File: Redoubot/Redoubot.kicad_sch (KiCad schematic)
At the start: 4 parts, among them U1 STM32G431RBTx, Y1 8MHz

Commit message: Added the footprints for the resistors, inductors and the crystal
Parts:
- Y1: footprint (none) -> Crystal:Crystal_SMD_HC49-SD
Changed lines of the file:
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@@
 			)
 		)
-		(property "Footprint" ""
+		(property "Footprint" "Crystal:Crystal_SMD_HC49-SD"
 			(at 34.29 49.53 0)
 			(hide yes)

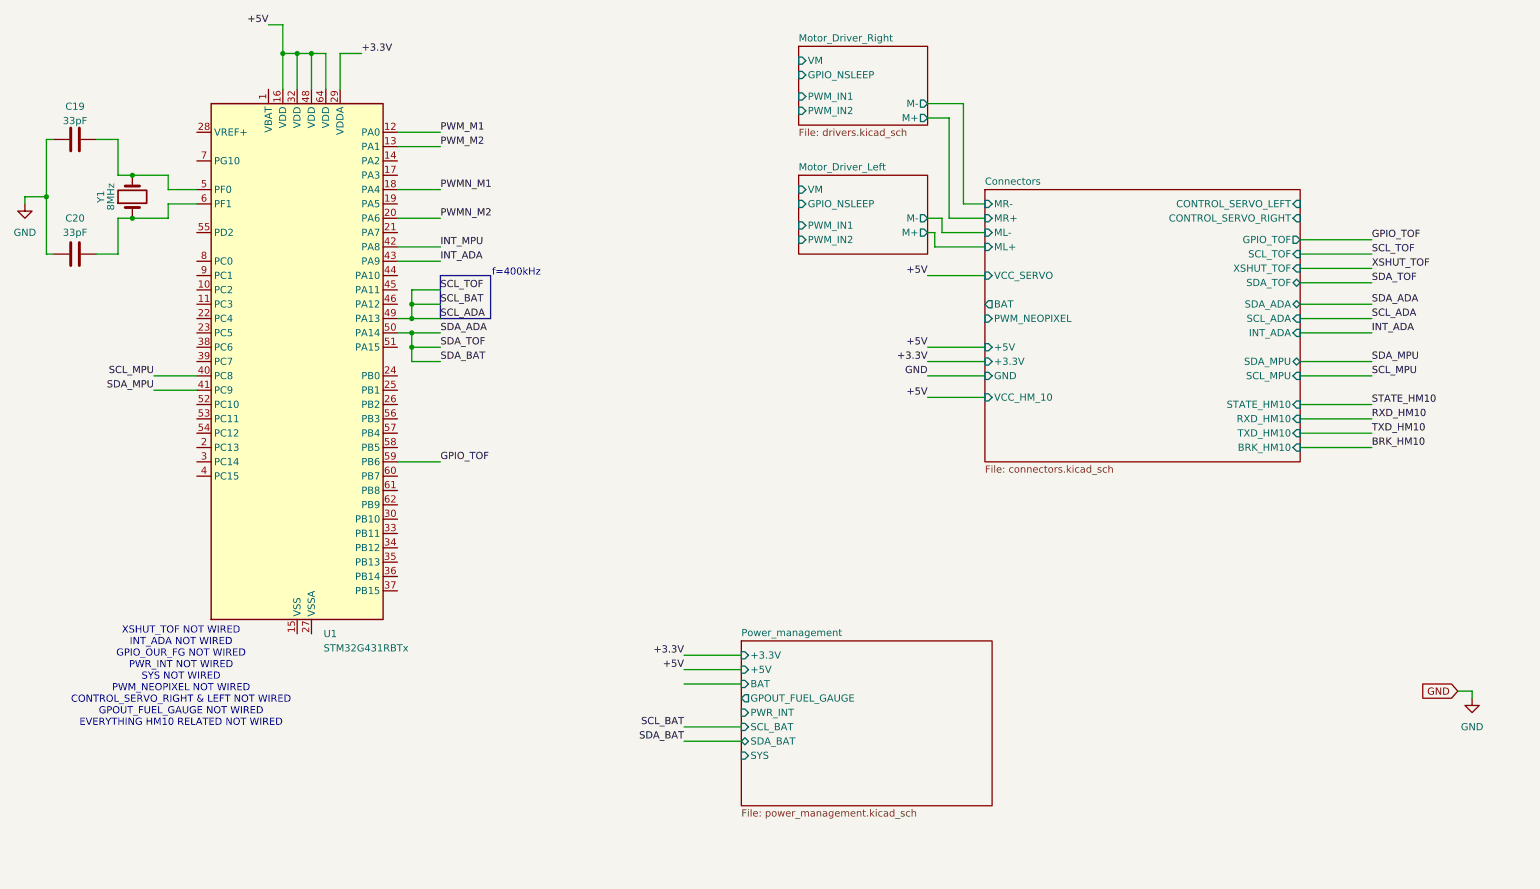
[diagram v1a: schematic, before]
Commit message: feat: added usb_c charging + flashing, added +3.3V generation, added HM10 & DFMini Support, wired everything and modified ioc accordingly
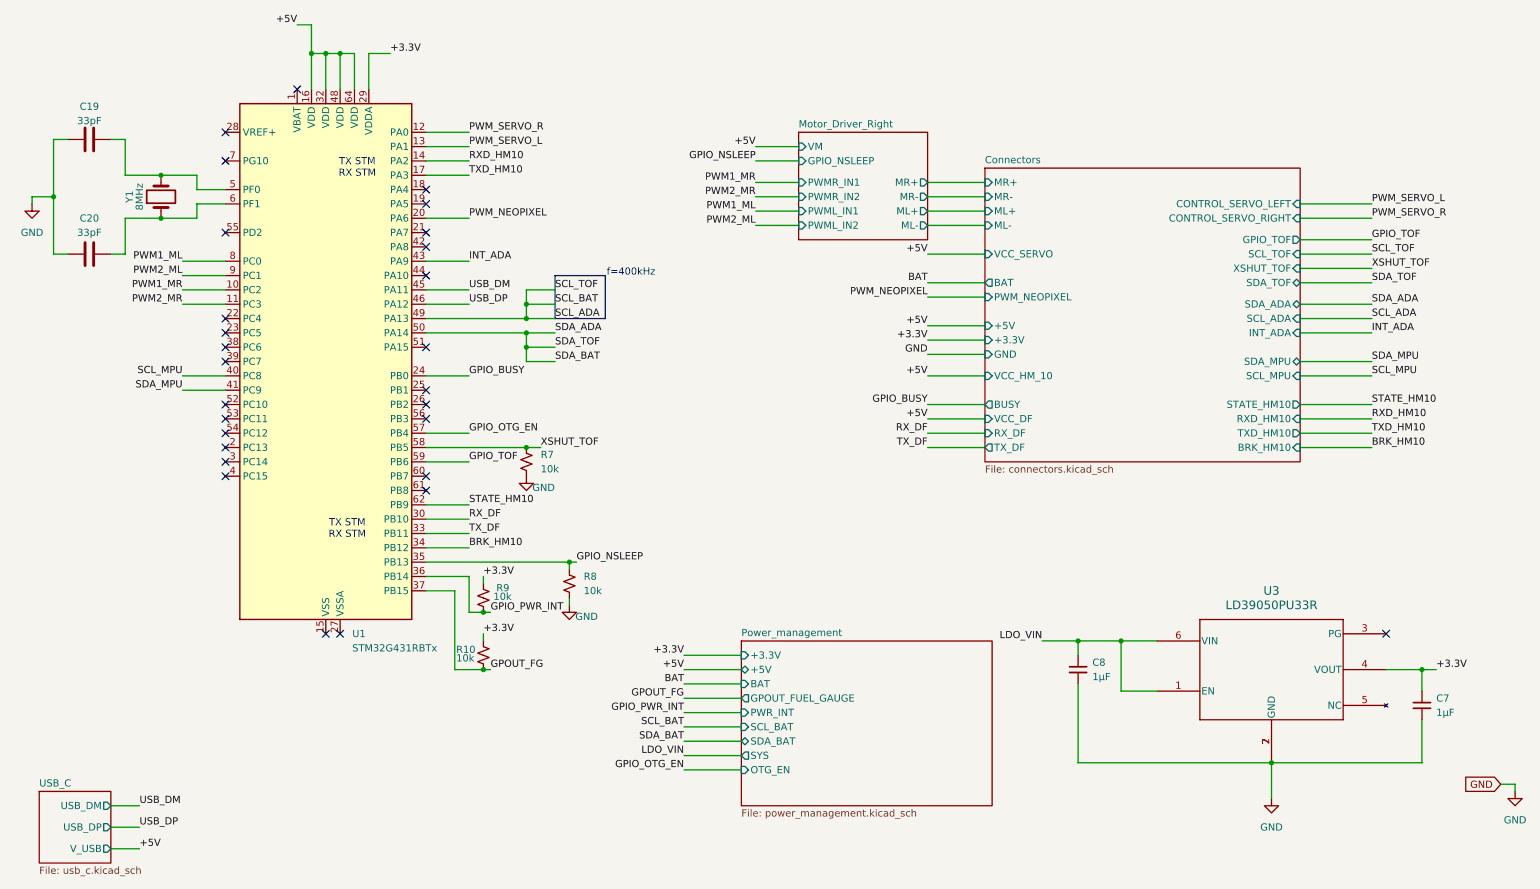
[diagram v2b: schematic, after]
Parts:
- added C7: 1µF, DFN6_3X3_STM, symbol Device:C_Small
- added C8: 1µF, symbol Device:C_Small
- added R10, R7, R8, R9: 10k, symbol Device:R_Small_US
- added U3: LD39050PU33R, DFN6_3X3_STM, symbol LD39050PU33R:LD39050PU33R
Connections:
- net +3.3V: now also C7.1, R10.1, R9.1, U3.4 (VOUT)
- net BRK_HM10: now also U1.34 (PB12)
- net GND: now also C7.2, C8.2, R7.2, R8.2, U3.2 (GND), U3.7 (GND)
- net RXD_HM10: now also U1.14 (PA2)
- net STATE_HM10: now also U1.62 (PB9)
- net TXD_HM10: now also U1.17 (PA3)
- net XSHUT_TOF: now also U1.58 (PB5), R7.1
- net PWM1_MR: now reaches U1.10 (PC2)
- net PWM2_MR: now reaches U1.11 (PC3)
- net GPIO_BUSY: now reaches U1.24 (PB0)
- net RX_DF: now reaches U1.30 (PB10)
- net TX_DF: now reaches U1.33 (PB11)
- net GPIO_NSLEEP: now reaches U1.35 (PB13)
- net GPIO_NSLEEP: now also R8.1
- net GPIO_PWR_INT: now reaches U1.36 (PB14)
- net GPIO_PWR_INT: now also R9.2
- net GPOUT_FG: now reaches U1.37 (PB15)
- net GPOUT_FG: now also R10.2
- net USB_DM: now reaches U1.45 (PA11)
- net USB_DP: now reaches U1.46 (PA12)
- net GPIO_OTG_EN: now reaches U1.57 (PB4)
- net PWM1_ML: now reaches U1.8 (PC0)
- net PWM2_ML: now reaches U1.9 (PC1)
- net INT_MPU: no longer names the net of U1.42 (PA8)
- net PWMN_M1: no longer names the net of U1.18 (PA4)
- net PWMN_M2 renamed PWM_NEOPIXEL
- net PWM_M1 renamed PWM_SERVO_R
- net PWM_M2 renamed PWM_SERVO_L
- new net LDO_VIN: C8.1, U3.1 (EN), U3.6 (VIN)
- no-connect marks 0 -> 28
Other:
- removed sheet Motor_Driver_Left
- added sheet USB_C (usb_c.kicad_sch)
- sheet Connectors ports: added BUSY, RX_DF, TX_DF, VCC_DF; removed none
- sheet Motor_Driver_Right ports: added ML+, ML-, MR+, MR-, PWML_IN1, PWML_IN2, PWMR_IN1, PWMR_IN2; removed M+, M-, PWM_IN1, PWM_IN2
- sheet Power_management ports: added OTG_EN; removed none
- note added: "TX STM RX STM"
- note removed: "XSHUT_TOF NOT WIRED INT_ADA NOT WIRED GPIO_OUR_FG NOT WIRED PWR_INT NOT WIRED SYS NOT WIRED PWM_NEOPIXEL NOT WIRED CONTROL_SERVO_RIGHT & LEFT NOT WIRED GPOUT_FUEL_GAUGE NOT WIRED EVERYTHING HM10 RELATED NOT WIRED"
- moved on the sheet: C19, C20, U1, Y1

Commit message: chore: added jumpers, changed 5v stm input to 3v3
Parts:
- added JP2: JMP_LDO_in, Jumper:SolderJumper-2_P1.3mm_Open_TrianglePad1.0x1.5mm, symbol Jumper:SolderJumper_2_Open
- added JP3: JMP_LDO_out, Jumper:SolderJumper-2_P1.3mm_Open_TrianglePad1.0x1.5mm, symbol Jumper:SolderJumper_2_Open
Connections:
- net +3.3V: now also U1.16 (VDD), U1.32 (VDD), U1.48 (VDD), U1.64 (VDD), JP3.1 (A); no longer C7.1, U3.4 (VOUT)
- net +5V: no longer U1.16 (VDD), U1.32 (VDD), U1.48 (VDD), U1.64 (VDD)
- net LDO_VIN: now also JP2.2 (B); no longer C8.1, U3.1 (EN), U3.6 (VIN)
- new net: C7.1, JP3.2 (B), U3.4 (VOUT)
- new net: C8.1, JP2.1 (A), U3.1 (EN), U3.6 (VIN)

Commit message: replaced the footprints for resistors with 0402 variants
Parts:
- removed JP2: JMP_LDO_in, Jumper:SolderJumper-2_P1.3mm_Open_TrianglePad1.0x1.5mm, symbol Jumper:SolderJumper_2_Open
- removed JP3: JMP_LDO_out, Jumper:SolderJumper-2_P1.3mm_Open_TrianglePad1.0x1.5mm, symbol Jumper:SolderJumper_2_Open
- C7, U3: footprint DFN6_3X3_STM -> footprints_LD39:DFN6_3X3_STM
- R10, R7, R8, R9: footprint (none) -> Resistor_SMD:R_0402_1005Metric
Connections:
- net +3.3V: now also C7.1, U3.4 (VOUT); no longer U1.16 (VDD), U1.32 (VDD), U1.48 (VDD), U1.64 (VDD)
- net +5V: now also U1.16 (VDD), U1.32 (VDD), U1.48 (VDD), U1.64 (VDD)
- net LDO_VIN: now also C8.1, U3.1 (EN), U3.6 (VIN)
